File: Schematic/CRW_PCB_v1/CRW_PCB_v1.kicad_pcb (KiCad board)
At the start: 2 copper layers, 3 parts

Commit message: Schematic work
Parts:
- removed REF**: DEV-16771, Teensy4_1:DEV-16771
- removed REF**: LGA28R50P4X10_380X520X100, BNO055:LGA28R50P4X10_380X520X100
- removed REF**: PQFN50P200X200X80-10N, BMP388:PQFN50P200X200X80-10N
- added BAT1: 1048P, 18650_Holder:BAT_1048P, F.Cu at (64.8, 45.7)
- added MCU1: TEENSY 4.1, Teensy4_1:DEV-16771, F.Cu at (58.4, 88.9)
- added U2: TPS62051DGS, CRW_PCB_v1:TPS62051DGS_VSSOP, F.Cu at (175.3, 113.0)
- added U3: BMP388, BMP388:PQFN50P200X200X80-10N, F.Cu at (146.4, 81.9)
- added U4: BNO055, BNO055:LGA28R50P4X10_380X520X100, F.Cu at (84.2, 102.2)
- added U6: TPS62051DGS, CRW_PCB_v1:TPS62051DGS_VSSOP, F.Cu at (182.1, 113.0)
- added XBEE1: XBEE Wire, XBEE:DIP2200W51P200L3294H279Q20P, F.Cu at (181.4, 56.1)

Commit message: Finished Schematic
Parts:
- removed BAT1: 1048P, 18650_Holder:BAT_1048P
- added U1: TPS62051DGS, CRW_PCB_v1:TPS62051DGS_VSSOP, F.Cu at (85.9, 80.5)
- added U5: DRV8838DSGR, CRW_PCB_v1:DRV8838DSGR, F.Cu at (166.6, 118.2)
- added U7: BNO055, BNO055:LGA28R50P4X10_380X520X100, F.Cu at (113.2, 68.3)
- U3: value BMP388 -> DRV8838DSGR; footprint BMP388:PQFN50P200X200X80-10N -> CRW_PCB_v1:DRV8838DSGR
- U4: value BNO055 -> DRV8838DSGR; footprint BNO055:LGA28R50P4X10_380X520X100 -> CRW_PCB_v1:DRV8838DSGR
- U6: value TPS62051DGS -> BMP388; footprint CRW_PCB_v1:TPS62051DGS_VSSOP -> BMP388:PQFN50P200X200X80-10N
- moved U2 92.0 mm to (85.8, 91.7), turned to 90 degrees
- moved U4 74.4 mm to (156.8, 118.8)
- moved U6 74.4 mm to (125.1, 65.2)
- moved MCU1 63.7 mm to (122.1, 86.6)
- moved XBEE1 50.6 mm to (193.0, 105.4)
- moved U3 36.6 mm to (144.3, 118.5)
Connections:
- net Net-(MCU1-PadD10) renamed CAM1_SS
- net Net-(MCU1-PadD11) renamed SPI_MOSI
- net Net-(MCU1-PadD12) renamed SPI_MISO
- net Net-(MCU1-PadD13/LED) renamed SPI_SCLK
- net Net-(MCU1-PadD22/A8) renamed BATT_ADC
- net Net-(MCU1-PadD23/A9) renamed THERM_ADC
- net Net-(MCU1-PadD36) renamed CAM2_SS
- net Net-(MCU1-PadD37) renamed CAM3_SS
- net Net-(U3-Pad5) renamed LEVEL1_PWM
- net Net-(U3-Pad6) renamed LEVEL1_DIR
- net Net-(U3-Pad7) renamed LEVEL1_~SLEEP
- net Net-(U4-Pad5) renamed LEVEL2_PWM
- net Net-(U4-Pad6) renamed LEVEL2_DIR
- net Net-(XBEE1-Pad5) renamed XBEE_~RESET
- MCU1 pad D14/A0: Net-(MCU1-PadD14/A0) -> BMP_INT
- MCU1 pad D15/A1: Net-(MCU1-PadD15/A1) -> BMP_ADDR_SEL
- MCU1 pad D16/A2: Net-(MCU1-PadD16/A2) -> IMU_INT
- MCU1 pad D17/A3: Net-(MCU1-PadD17/A3) -> IMU_ADDR_SEL
- MCU1 pad D18/A4: Net-(MCU1-PadD18/A4) -> I2C_SDA
- MCU1 pad D19/A5: Net-(MCU1-PadD19/A5) -> I2C_SCL
- MCU1 pad D7: Net-(MCU1-PadD7) -> XBEE_UART_MISO
- MCU1 pad D8: Net-(MCU1-PadD8) -> XBEE_UART_MOSI
- U3 pad 1: Net-(U3-Pad1) -> +BATT
- U3 pad 3: Net-(U3-Pad3) -> Net-(J2-Pad2)
- U3 pad 4: Net-(U3-Pad4) -> Net-(C1-Pad2)
- U3 pad 8: Net-(U3-Pad3) -> +3V3
- U3 pad 9: Net-(U3-Pad3) -> (no net)
- U4 pad 1: (no net) -> +BATT
- U4 pad 4: Net-(U4-Pad4) -> Net-(C1-Pad2)
- U4 pad 7: (no net) -> LEVEL2_~SLEEP
- U4 pad 8: (no net) -> +3V3
- U4 pad 9: Net-(U4-Pad9) -> (no net)
- U6 pad 1: +BATT -> +3V3
- U6 pad 10: -BATT -> +3V3
- U6 pad 2: Net-(R10-Pad2) -> I2C_SCL
- U6 pad 4: Net-(R9-Pad2) (its old number) -> I2C_SDA
- U6 pad 5: Net-(Cff2-Pad2) (its old number) -> BMP_ADDR_SEL
- U6 pad 6: Net-(R7-Pad2) (its old number) -> +3V3
- U6 pad 7: -BATT -> BMP_INT
- U6 pad 8: +BATT -> -BATT
- U6 pad 9: Net-(L2-Pad1) (its old number) -> -BATT
- XBEE1 pad 2: Net-(XBEE1-Pad2) -> XBEE_UART_MISO
- XBEE1 pad 3: Net-(XBEE1-Pad3) -> XBEE_UART_MOSI

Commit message: Removed .lib from .gitignore
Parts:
- added C1: 0.1uF, Capacitor_SMD:C_0603_1608Metric_Pad1.08x0.95mm_HandSolder, F.Cu at (32.0, 34.1)
- added C10: 120nF, Capacitor_SMD:C_0603_1608Metric_Pad1.08x0.95mm_HandSolder, F.Cu at (313.9, 124.3)
- added C11: 0.1uF, Capacitor_SMD:C_0603_1608Metric_Pad1.08x0.95mm_HandSolder, F.Cu at (312.2, 117.2)
- added C2: 0.1uF, Capacitor_SMD:C_0603_1608Metric_Pad1.08x0.95mm_HandSolder, F.Cu at (33.5, 34.0)
- added C3: 0.1uF, Capacitor_SMD:C_0603_1608Metric_Pad1.08x0.95mm_HandSolder, F.Cu at (43.0, 34.3)
- added C4: 0.1uF, Capacitor_SMD:C_0603_1608Metric_Pad1.08x0.95mm_HandSolder, F.Cu at (44.5, 34.3)
- added C5: 0.1uF, Capacitor_SMD:C_0603_1608Metric_Pad1.08x0.95mm_HandSolder, F.Cu at (53.9, 34.1)
- added C6: 0.1uF, Capacitor_SMD:C_0603_1608Metric_Pad1.08x0.95mm_HandSolder, F.Cu at (55.4, 34.1)
- added C7: 0.1uF, Capacitor_SMD:C_0603_1608Metric_Pad1.08x0.95mm_HandSolder, F.Cu at (297.6, 123.7)
- added C8: 1uF, Capacitor_SMD:C_0603_1608Metric_Pad1.08x0.95mm_HandSolder, F.Cu at (317.5, 126.9)
- added C9: 0.1uF, Capacitor_SMD:C_0603_1608Metric_Pad1.08x0.95mm_HandSolder, F.Cu at (294.5, 126.7)
- added CAM1: CAMERA, Connector_JST:JST_SH_BM06B-SRSS-TB_1x06-1MP_P1.00mm_Vertical, F.Cu at (254.0, 190.5)
- added CAM2: CAMERA, Connector_JST:JST_SH_BM06B-SRSS-TB_1x06-1MP_P1.00mm_Vertical, F.Cu at (266.7, 190.5)
- added CAM3: CAMERA, Connector_JST:JST_SH_BM06B-SRSS-TB_1x06-1MP_P1.00mm_Vertical, F.Cu at (279.4, 190.5)
- added Cff1: 6.8pF, Capacitor_SMD:C_0402_1005Metric_Pad0.74x0.62mm_HandSolder, F.Cu at (179.6, 71.3)
- added Cff2: 6.8pF, Capacitor_SMD:C_0402_1005Metric_Pad0.74x0.62mm_HandSolder, F.Cu at (124.7, 118.0)
- added Ci1: 10uF, Capacitor_SMD:C_0805_2012Metric_Pad1.18x1.45mm_HandSolder, F.Cu at (164.2, 46.8)
- added Ci2: 10uF, Capacitor_SMD:C_0805_2012Metric_Pad1.18x1.45mm_HandSolder, F.Cu at (120.6, 96.5)
- added Co1: 22uF, Capacitor_SMD:C_0805_2012Metric_Pad1.18x1.45mm_HandSolder, F.Cu at (200.0, 71.2)
- added Co2: 22uF, Capacitor_SMD:C_0805_2012Metric_Pad1.18x1.45mm_HandSolder, F.Cu at (134.1, 114.6)
- added D1: D_Zener, Diode_SMD:D_SOD-123, F.Cu at (164.8, 157.2)
- added D2: D_Schottky, Diode_SMD:D_SMB, F.Cu at (163.2, 168.4)
- added D3: D_Schottky, Diode_SMD:D_SMB, F.Cu at (176.0, 171.9)
- added D4: FLYBACK, Diode_SMD:D_SMC, F.Cu at (229.8, 126.8)
- added J1: BATTERIES, Connector_JST:JST_SH_BM02B-SRSS-TB_1x02-1MP_P1.00mm_Vertical, F.Cu at (173.9, 148.3)
- added J3: AUTOGYRO_RELEASE, Connector_JST:JST_SH_BM02B-SRSS-TB_1x02-1MP_P1.00mm_Vertical, F.Cu at (216.6, 129.6)
- added J4: GPS_Connector, Connector_JST:JST_SH_BM03B-SRSS-TB_1x03-1MP_P1.00mm_Vertical, F.Cu at (292.8, 191.1)
- added J6: QWIIC_Connector, Connector_JST:JST_SH_BM04B-SRSS-TB_1x04-1MP_P1.00mm_Vertical, F.Cu at (281.6, 135.4)
- added L1: 10uH, Inductor_SMD:L_Taiyo-Yuden_NR-60xx, F.Cu at (201.5, 47.0)
- added L2: 10uH, Inductor_SMD:L_Taiyo-Yuden_NR-60xx, F.Cu at (157.3, 101.2)
- added MTR1: LEVEL1, Connector_JST:JST_SH_BM02B-SRSS-TB_1x02-1MP_P1.00mm_Vertical, F.Cu at (30.6, 29.7)
- added MTR2: LEVEL2, Connector_JST:JST_SH_BM02B-SRSS-TB_1x02-1MP_P1.00mm_Vertical, F.Cu at (41.8, 30.0)
- added MTR3: LEVEL3, Connector_JST:JST_SH_BM02B-SRSS-TB_1x02-1MP_P1.00mm_Vertical, F.Cu at (52.6, 29.8)
- added Q1: Q_PMOS_GSD, Package_TO_SOT_SMD:SC-59_Handsoldering, F.Cu at (175.1, 163.8)
- added Q2: Q_PMOS_GSD, Package_TO_SOT_SMD:SC-59_Handsoldering, F.Cu at (184.8, 159.3)
- added Q3: Q_NMOS_GSD, Package_TO_SOT_SMD:SC-59_Handsoldering, F.Cu at (223.1, 135.9)
- added Q4: Q_NMOS_GSD, Package_TO_SOT_SMD:SC-59_Handsoldering, F.Cu at (244.4, 180.4)
- added R1: 10k, Resistor_SMD:R_0402_1005Metric_Pad0.72x0.64mm_HandSolder, F.Cu at (163.3, 151.5)
- added R10: 10k, Resistor_SMD:R_0402_1005Metric_Pad0.72x0.64mm_HandSolder, F.Cu at (181.3, 154.4)
- added R11: 560k, Resistor_SMD:R_0402_1005Metric_Pad0.72x0.64mm_HandSolder, F.Cu at (184.1, 76.5)
- added R12: 100k, Resistor_SMD:R_0402_1005Metric_Pad0.72x0.64mm_HandSolder, F.Cu at (185.2, 69.4)
- added R13: 820k, Resistor_SMD:R_0402_1005Metric_Pad0.72x0.64mm_HandSolder, F.Cu at (145.4, 130.1)
- added R14: 91k, Resistor_SMD:R_0402_1005Metric_Pad0.72x0.64mm_HandSolder, F.Cu at (151.9, 120.5)
- added R15: 220, Resistor_SMD:R_0603_1608Metric_Pad0.98x0.95mm_HandSolder, F.Cu at (211.0, 125.1)
- added R16: 10k, Resistor_SMD:R_0402_1005Metric_Pad0.72x0.64mm_HandSolder, F.Cu at (216.5, 136.0)
- added R17: 10k, Resistor_SMD:R_0402_1005Metric_Pad0.72x0.64mm_HandSolder, F.Cu at (33.0, 43.1)
- added R18: 10k, Resistor_SMD:R_0402_1005Metric_Pad0.72x0.64mm_HandSolder, F.Cu at (58.7, 41.0)
- added R19: 4.7k, Resistor_SMD:R_0402_1005Metric_Pad0.72x0.64mm_HandSolder, F.Cu at (249.4, 183.4)
- added R2: 130k, Resistor_SMD:R_0402_1005Metric_Pad0.72x0.64mm_HandSolder, F.Cu at (191.1, 52.2)
- added R20: 4.7k, Resistor_SMD:R_0402_1005Metric_Pad0.72x0.64mm_HandSolder, F.Cu at (260.2, 183.1)
- added R21: 4.7k, Resistor_SMD:R_0402_1005Metric_Pad0.72x0.64mm_HandSolder, F.Cu at (273.2, 183.3)
- added R22: 10k, Resistor_SMD:R_0402_1005Metric_Pad0.72x0.64mm_HandSolder, F.Cu at (75.3, 44.8)
- added R23: 220, Resistor_SMD:R_0603_1608Metric_Pad0.98x0.95mm_HandSolder, F.Cu at (251.0, 169.5)
- added R24: 4.7k, Resistor_SMD:R_0402_1005Metric_Pad0.72x0.64mm_HandSolder, F.Cu at (283.8, 126.1)
- added R25: 47k, Resistor_SMD:R_0402_1005Metric_Pad0.72x0.64mm_HandSolder, F.Cu at (248.8, 112.8)
- added R26: 10k, Resistor_SMD:R_0402_1005Metric_Pad0.72x0.64mm_HandSolder, F.Cu at (248.7, 174.5)
- added R27: 10k, Resistor_SMD:R_0402_1005Metric_Pad0.72x0.64mm_HandSolder, F.Cu at (308.3, 159.5)
- added R28: 4.7k, Resistor_SMD:R_0402_1005Metric_Pad0.72x0.64mm_HandSolder, F.Cu at (278.3, 124.7)
- added R29: 10k, Resistor_SMD:R_0402_1005Metric_Pad0.72x0.64mm_HandSolder, F.Cu at (301.7, 130.5)
- added R3: 100k, Resistor_SMD:R_0402_1005Metric_Pad0.72x0.64mm_HandSolder, F.Cu at (194.5, 58.0)
- added R30: 100k, Resistor_SMD:R_0402_1005Metric_Pad0.72x0.64mm_HandSolder, F.Cu at (242.3, 76.0)
- added R31: 47k, Resistor_SMD:R_0402_1005Metric_Pad0.72x0.64mm_HandSolder, F.Cu at (245.9, 75.8)
- added R32: 10k, Resistor_SMD:R_0402_1005Metric_Pad0.72x0.64mm_HandSolder, F.Cu at (306.5, 132.0)
- added R4: 130k, Resistor_SMD:R_0402_1005Metric_Pad0.72x0.64mm_HandSolder, F.Cu at (156.5, 118.1)
- added R5: 100k, Resistor_SMD:R_0402_1005Metric_Pad0.72x0.64mm_HandSolder, F.Cu at (139.0, 108.8)
- added R6: 1M, Resistor_SMD:R_0402_1005Metric_Pad0.72x0.64mm_HandSolder, F.Cu at (164.9, 79.6)
- added R7: 1M, Resistor_SMD:R_0402_1005Metric_Pad0.72x0.64mm_HandSolder, F.Cu at (134.0, 131.0)
- added R8: 1M, Resistor_SMD:R_0402_1005Metric_Pad0.72x0.64mm_HandSolder, F.Cu at (190.7, 76.0)
- added R9: 1M, Resistor_SMD:R_0402_1005Metric_Pad0.72x0.64mm_HandSolder, F.Cu at (103.2, 108.8)
- added TH1: Thermistor, Resistor_THT:R_Axial_DIN0204_L3.6mm_D1.6mm_P2.54mm_Vertical, F.Cu at (247.9, 109.2)
- moved U7 199.5 mm to (304.5, 125.2)
- moved U6 179.3 mm to (294.5, 123.7), turned to 180 degrees
- moved MCU1 157.2 mm to (264.4, 153.6)
- moved U4 144.6 mm to (39.6, 34.1), turned to 270 degrees
- moved U5 143.5 mm to (50.4, 33.9), turned to 270 degrees
- moved U3 143.5 mm to (28.5, 33.8), turned to 270 degrees
- moved XBEE1 141.0 mm to (322.7, 160.9)
- moved U1 104.9 mm to (185.7, 48.1), turned to 0 degrees
- moved U2 43.7 mm to (127.1, 106.1), turned to 0 degrees
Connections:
- MCU1 pad D14/A0: BMP_INT -> LEVEL1_PWM
- MCU1 pad D15/A1: BMP_ADDR_SEL -> LEVEL2_PWM
- MCU1 pad D16/A2: IMU_INT -> I2C_SDA
- MCU1 pad D17/A3: IMU_ADDR_SEL -> I2C_SCL
- MCU1 pad D18/A4: I2C_SDA -> LEVEL3_PWM
- MCU1 pad D19/A5: I2C_SCL -> LEVEL1_DIR
- MCU1 pad D20/A6: Net-(MCU1-PadD20/A6) -> LEVEL2_DIR
- MCU1 pad D21/A7: Net-(MCU1-PadD21/A7) -> LEVEL3_DIR
- MCU1 pad D25/A11: Net-(MCU1-PadD25/A11) -> GPS_UART_MISO
- MCU1 pad D28: Net-(MCU1-PadD28) -> XBEE_UART_MISO
- MCU1 pad D29: Net-(MCU1-PadD29) -> XBEE_UART_MOSI
- MCU1 pad D30: Net-(MCU1-PadD30) -> XBEE_~RESET
- MCU1 pad D33: Net-(MCU1-PadD33) -> LEVEL1_~SLEEP
- MCU1 pad D34: Net-(MCU1-PadD34) -> LEVEL2_~SLEEP
- MCU1 pad D35: Net-(MCU1-PadD35) -> LEVEL3_~SLEEP
- MCU1 pad D36: CAM2_SS -> GYRO_RELEASE
- MCU1 pad D37: CAM3_SS -> BMP_INT
- MCU1 pad D38/A14: Net-(MCU1-PadD38/A14) -> BMP_ADDR_SEL
- MCU1 pad D39/A15: Net-(MCU1-PadD39/A15) -> IMU_INT
- MCU1 pad D40/A16: Net-(MCU1-PadD40/A16) -> IMU_ADDR_SEL
- MCU1 pad D41/A17: Net-(MCU1-PadD41/A17) -> IMU_~RESET
- MCU1 pad D7: XBEE_UART_MISO -> CAM_PWR
- MCU1 pad D8: XBEE_UART_MOSI -> CAM3_SS
- MCU1 pad D9: Net-(MCU1-PadD9) -> CAM2_SS
- MCU1 pad VUSB: Net-(MCU1-PadVUSB) -> USB_PWR
- U3 pad 4: Net-(C1-Pad2) -> -BATT
- U4 pad 4: Net-(C1-Pad2) -> -BATT
- U5 pad 4: Net-(C1-Pad2) -> -BATT
- U7 pad 10: -BATT -> Net-(U7-Pad10)
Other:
- net class Default: clearance 0.2 -> 0.1524; trace_width 0.25 -> 0.1524; via_dia 0.8 -> 0.6858; via_drill 0.4 -> 0.3302
- rule pad_to_mask_clearance: 0 -> 0.0508
- rule trace_clearance: 0.2 -> 0.1524
- rule trace_min: 0.2 -> 0.1524
- rule via_min_drill: 0.3 -> 0.254
- rule via_min_size: 0.4 -> 0.508

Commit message: Maybe Finished PCB
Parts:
- removed MTR1: LEVEL1, Connector_JST:JST_SH_BM02B-SRSS-TB_1x02-1MP_P1.00mm_Vertical
- removed MTR2: LEVEL2, Connector_JST:JST_SH_BM02B-SRSS-TB_1x02-1MP_P1.00mm_Vertical
- removed MTR3: LEVEL3, Connector_JST:JST_SH_BM02B-SRSS-TB_1x02-1MP_P1.00mm_Vertical
- added J2: LEVEL1, Connector_JST:JST_SH_BM02B-SRSS-TB_1x02-1MP_P1.00mm_Vertical, F.Cu at (100.3, 29.5)
- added J5: LEVEL2, Connector_JST:JST_SH_BM02B-SRSS-TB_1x02-1MP_P1.00mm_Vertical, F.Cu at (92.4, 29.5)
- added J7: LEVEL3, Connector_JST:JST_SH_BM02B-SRSS-TB_1x02-1MP_P1.00mm_Vertical, F.Cu at (84.3, 29.4)
- moved J4 249.7 mm to (80.5, 59.6)
- moved CAM1 247.8 mm to (43.6, 59.6)
- moved CAM2 247.8 mm to (56.3, 59.6)
- moved CAM3 247.8 mm to (69.0, 59.6)
- moved R23 244.7 mm to (33.4, 57.7), turned to 90 degrees
- moved R26 243.4 mm to (33.4, 61.0), turned to 270 degrees
- moved Q4 240.9 mm to (36.1, 59.2), turned to 90 degrees
- moved R27 236.4 mm to (94.7, 58.1)
- moved R19 235.5 mm to (49.2, 59.5), turned to 270 degrees
- moved R21 233.8 mm to (74.7, 59.8), turned to 270 degrees
- moved R20 233.4 mm to (62.1, 59.7), turned to 270 degrees
- moved MCU1 232.4 mm to (58.2, 46.3)
- moved C8 232.0 mm to (97.6, 53.1), turned to 180 degrees
- moved C10 229.7 mm to (98.2, 45.4)
- moved C11 229.1 mm to (93.7, 48.2), turned to 90 degrees
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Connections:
- U3 pad 9: (no net) -> -BATT
- U4 pad 9: (no net) -> -BATT
- U5 pad 9: (no net) -> -BATT
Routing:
- net +3V3: track 0.00 -> 265.9 mm, vias 0 -> 11
- net +BATT: track 0.00 -> 158.0 mm, vias 0 -> 10
- net +5V: track 0.00 -> 103.3 mm, vias 0 -> 4
- net I2C_SCL: track 0.00 -> 85.1 mm, vias 0 -> 4
- net I2C_SDA: track 0.00 -> 81.9 mm, vias 0 -> 3
- net SPI_SCLK: track 0.00 -> 56.6 mm, vias 0 -> 5
- net LEVEL1_DIR: track 0.00 -> 56.0 mm, vias 0 -> 4
- net SPI_MOSI: track 0.00 -> 55.4 mm, vias 0 -> 5
- net -BATT: track 0.00 -> 55.0 mm, vias 0 -> 11
- net LEVEL2_DIR: track 0.00 -> 49.8 mm, vias 0 -> 2
- net LEVEL3_DIR: track 0.00 -> 45.7 mm
- net XBEE_UART_MISO: track 0.00 -> 44.9 mm, vias 0 -> 1
- net SPI_MISO: track 0.00 -> 44.8 mm, vias 0 -> 4
- net GYRO_RELEASE: track 0.00 -> 44.0 mm, vias 0 -> 1
- net XBEE_~RESET: track 0.00 -> 44.0 mm, vias 0 -> 1
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- added copper zone on B.Cu, net -BATT
- added copper zone on F.Cu, net -BATT
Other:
- board outline added: 114.3 x 38.1 mm
- net class 1A added: clearance 0.1524, trace_width 0.254, via_dia 0.6858, via_drill 0.3302
- rule trace_min: 0.1524 -> 0
- board text added: "UAH CRW PCB v1"

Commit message: Finished PCB v1
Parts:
- removed J6: QWIIC_Connector, Connector_JST:JST_SH_BM04B-SRSS-TB_1x04-1MP_P1.00mm_Vertical
- removed XBEE1: XBEE Wire, XBEE:DIP2200W51P200L3294H279Q20P
- added RANGE: QWIIC_Connector, Connector_JST:JST_SH_BM04B-SRSS-TB_1x04-1MP_P1.00mm_Vertical, F.Cu at (89.0, 59.7)
- added XBEE: XBEE Wire, XBEE:DIP2200W51P200L3294H279Q20P, F.Cu at (126.7, 45.9)
- moved Ci1 0.30 mm to (72.8, 27.6)
- moved Co1 0.13 mm to (77.0, 27.6)
- moved Ci2 0.13 mm to (57.3, 27.7)
- moved Co2 0.11 mm to (61.9, 27.7)
- renumbered J1 to BATT, J4 to GPS, MCU1 to MCU, J2 to MOTOR1, J5 to MOTOR2, J7 to MOTOR3, J3 to RELEASE
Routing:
- net -BATT: track 55.0 -> 13.9 mm, vias 11 -> 22
- net Net-(D2-Pad2): track 10.8 -> 8.53 mm
- net BATT_ADC: track 22.0 -> 20.3 mm
- net +5V: track 103.3 -> 104.2 mm, vias 4 -> 6
- net Net-(L1-Pad1): track 8.21 -> 7.42 mm
- net +3V3: track 265.9 -> 265.3 mm
- net THERM_ADC: track 33.5 -> 32.8 mm
- net Net-(L2-Pad1): track 8.27 -> 7.66 mm
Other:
- rule trace_min: 0 -> 0.1524

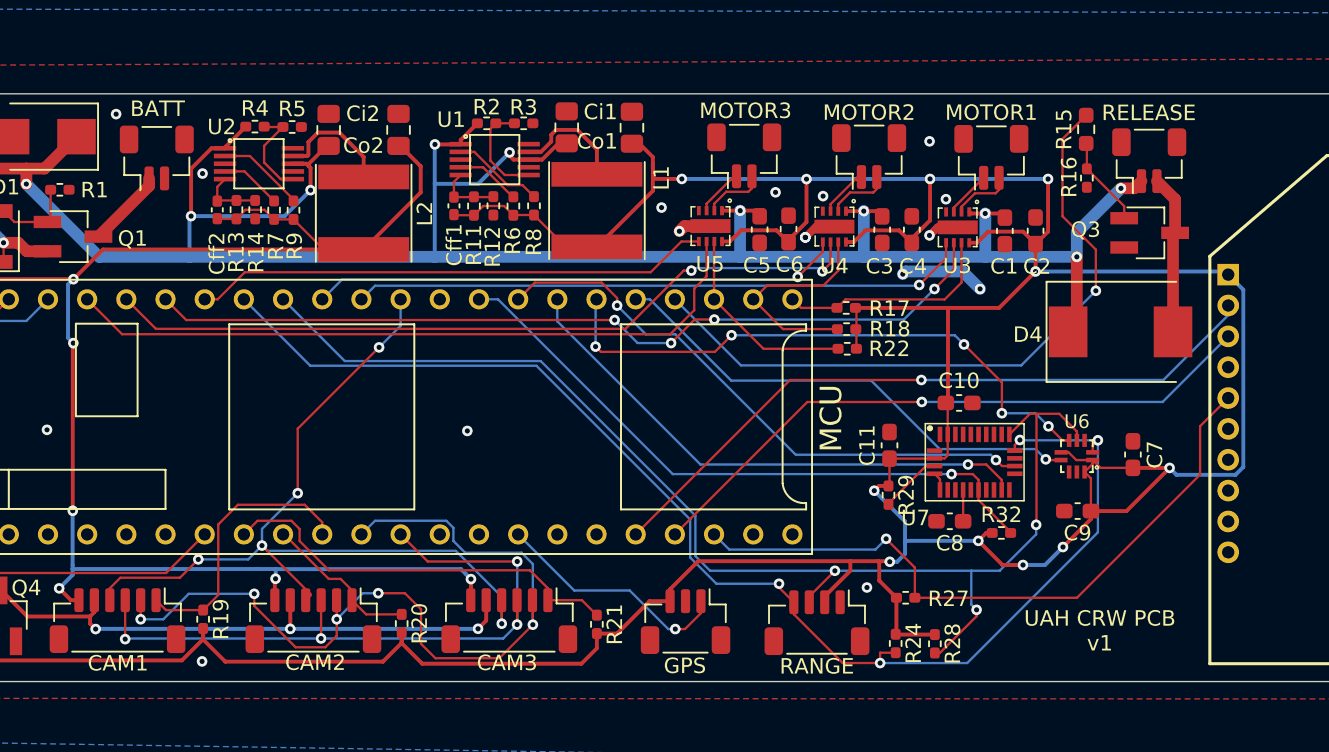
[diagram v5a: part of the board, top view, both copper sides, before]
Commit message: Change Power connectors
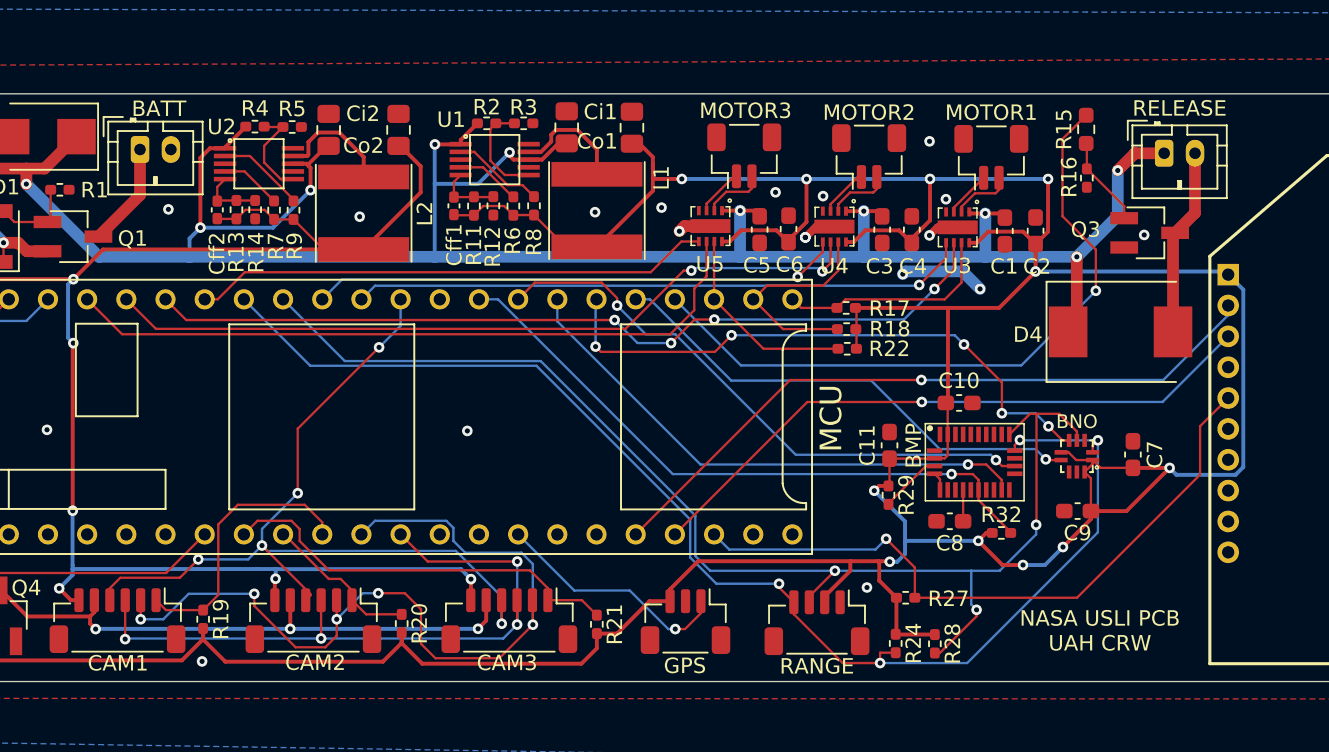
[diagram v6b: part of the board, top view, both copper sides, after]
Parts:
- removed the BATT at (46.2, 29.6)
- removed the RELEASE at (110.5, 29.7)
- added BATT: BATTERIES, Connector_JST:JST_PH_B2B-PH-K_1x02_P2.00mm_Vertical, F.Cu at (45.1, 29.0)
- added RELEASE: AUTOGYRO_RELEASE, Connector_JST:JST_PH_B2B-PH-K_1x02_P2.00mm_Vertical, F.Cu at (111.5, 29.3)
- renumbered U7 to BMP, U6 to BNO
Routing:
- net +BATT: track 158.1 -> 160.9 mm
- net Net-(D4-Pad2): track 10.3 -> 12.2 mm
- net Net-(BATT1-Pad1): track 5.13 -> 6.76 mm
- net -BATT: vias 22 -> 24
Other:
- board text added: "Design: v1 Creator: Patrick Smith"
- board text added: "NASA USLI PCB UAH CRW"
- board text removed: "UAH CRW PCB v1"

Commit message: Used Hierarchical Sheets
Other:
- board text added: "Design: v1"
- board text removed: "Design: v1 Creator: Patrick Smith"
